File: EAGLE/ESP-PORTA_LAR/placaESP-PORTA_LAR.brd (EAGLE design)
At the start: 53.3 x 42.9 mm, 21 parts

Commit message: Correções na placa da porta
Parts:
- R1, R2, R3, R4, R5, R6, R7, R8: device resistor:0204/7 -> resistor:0207/10
- moved R7 13.9 mm to (44.2, 9.14)
- moved RESET 4.87 mm to (41.3, 20.1)
- moved FTDI 4.55 mm to (42.5, 38.7)
- moved FLASH 4.51 mm to (41.1, 28.6)
- moved MRFC522 2.57 mm to (49.1, 22.9)
- moved R8 2.43 mm to (32.0, 15.4)
- moved R4 1.73 mm to (6.86, 34.7)
- moved R2 1.65 mm to (3.81, 34.7)
- moved R5 1.05 mm to (32.0, 9.14)
- moved R3 0.74 mm to (31.1, 23.7)
- moved R6 0.57 mm to (32.0, 12.2)
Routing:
- net LED3: track 13.8 -> 36.3 mm
- net VCC: track 120.2 -> 104.1 mm
- net MISO: track 56.4 -> 40.7 mm, vias 1 -> 2
- net MOSI: track 37.4 -> 25.3 mm, vias 0 -> 1
- net CTS: track 65.5 -> 76.7 mm
- net RST: track 25.3 -> 35.7 mm, vias 0 -> 1
- net LED1: track 35.4 -> 43.4 mm
- net N$7: track 14.8 -> 7.53 mm
- net N$8: track 23.6 -> 16.4 mm
- net SDA: track 73.6 -> 80.5 mm, vias 1 -> 2
- net SCK: track 62.1 -> 67.2 mm
- net RXI: track 22.1 -> 25.8 mm
- net N$3: track 10.6 -> 13.0 mm
- net LED4: track 12.2 -> 10.6 mm
- net N$5: track 6.84 -> 8.39 mm
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
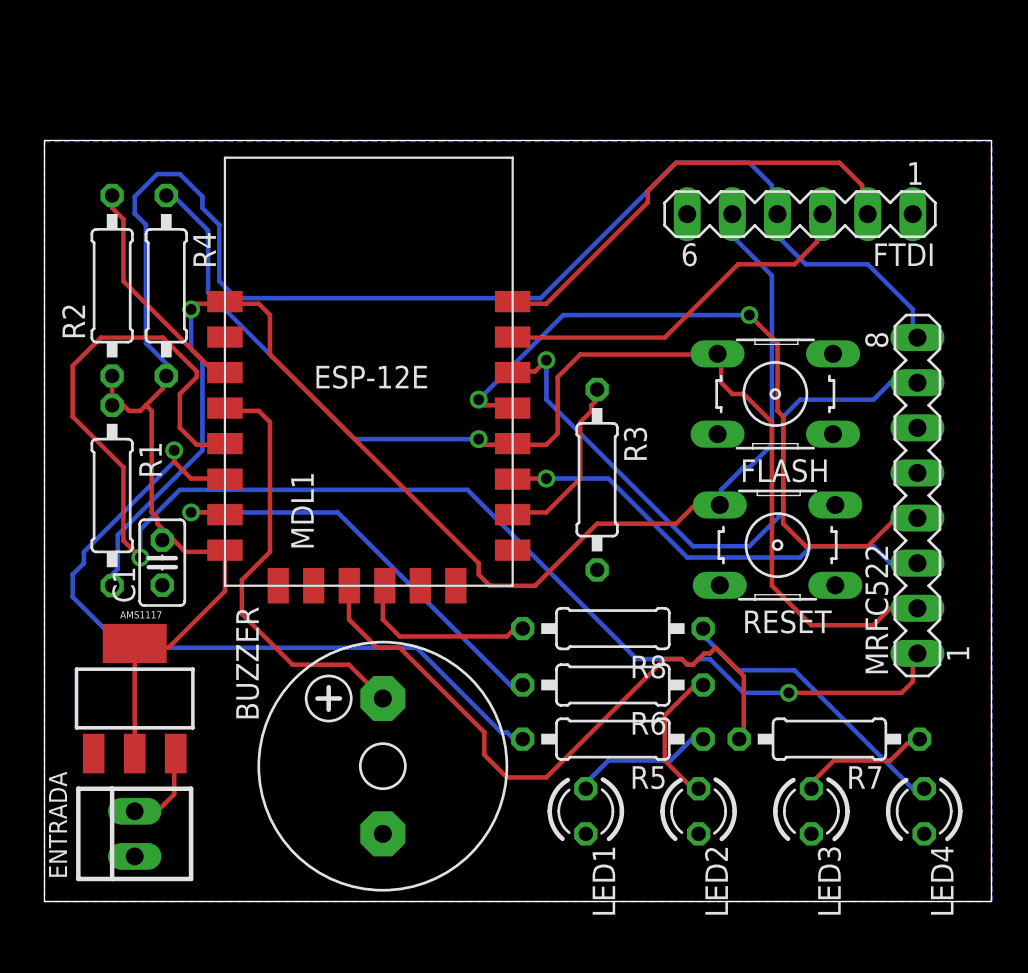
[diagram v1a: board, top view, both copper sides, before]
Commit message: Mudanças na placa
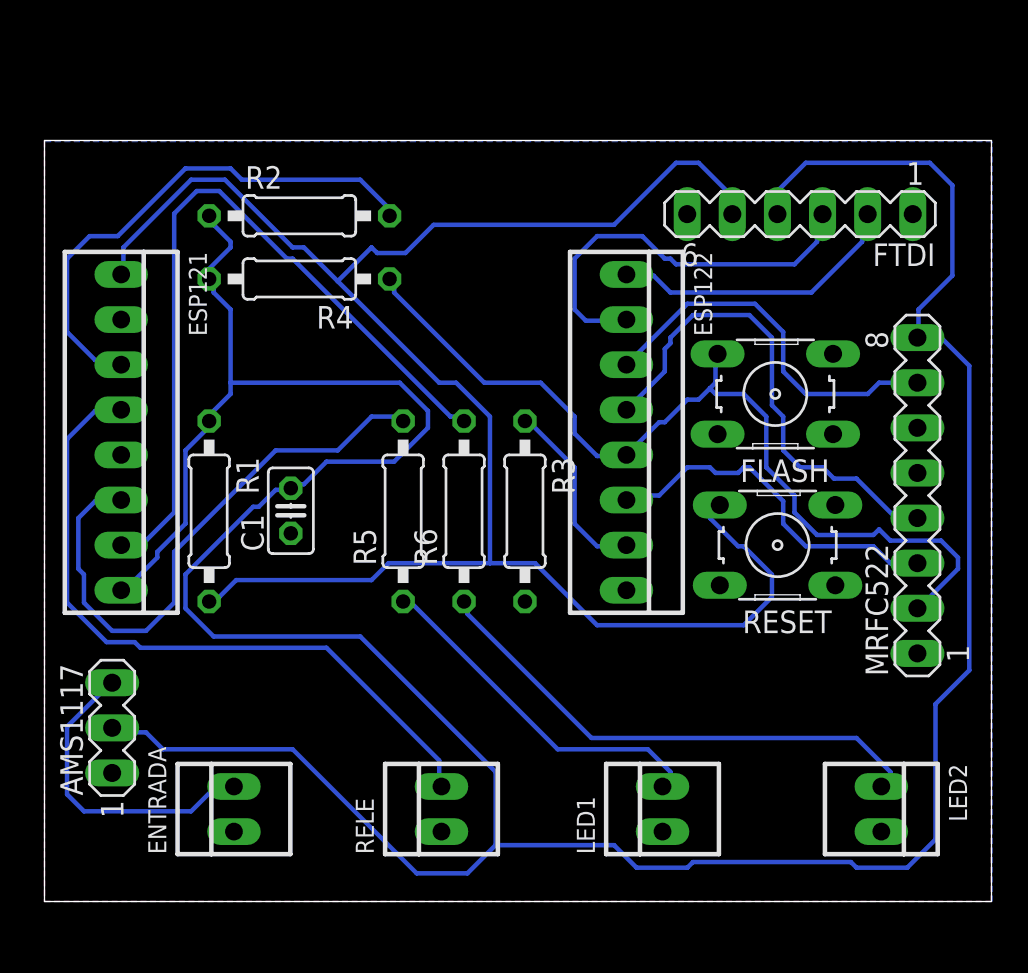
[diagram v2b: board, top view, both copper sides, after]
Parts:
- removed BUZZER: F/CM12P, buzzer:F/CM12P
- removed LED3, LED4: (no value), led:LED3MM
- removed MDL1: (no value), ESP8266-ESP12E:ESP8266-ESP12E
- removed R7, R8: 220R, resistor:0207/10
- added ESP121: Dir, con-molex:22-23-2081
- added ESP122: Esq, con-molex:22-23-2081
- added RELE: 2, con-molex:22-23-2021
- AMS1117: device kaibader:AMS1117 -> con-lstb:MA03-1
- ENTRADA: value 22-23-2021 -> 1
- LED1: value (none) -> 3; device led:LED3MM -> con-molex:22-23-2021
- LED2: value (none) -> 4; device led:LED3MM -> con-molex:22-23-2021
- moved R5 17.4 mm to (20.2, 22.0), turned to 90 degrees
- moved R6 12.9 mm to (23.6, 22.0), turned to 90 degrees
- moved R2 11.3 mm to (14.4, 38.6), turned to 0 degrees
- moved LED2 10.3 mm to (47.1, 5.21)
- moved C1 7.81 mm to (13.9, 22.0)
- moved R4 7.50 mm to (14.4, 35.1), turned to 180 degrees
- moved ENTRADA 5.76 mm to (10.7, 5.21)
- moved R1 5.53 mm to (9.27, 22.0)
- moved R3 4.44 mm to (27.1, 22.0)
- moved LED1 4.32 mm to (34.8, 5.21), turned to 90 degrees
- moved AMS1117 2.08 mm to (3.81, 9.78), turned to 90 degrees
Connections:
- removed net BUZZ: BUZZER.+, MDL1.4
- removed net LED3: MDL1.19, R7.2
- removed net LED4: MDL1.20, R8.2
- removed net N$7: LED3.A, R7.1
- removed net N$8: LED4.A, R8.1
- new net RELE: ESP121.4, RELE.2
- net CTS: now also ESP121.1; no longer MDL1.1
- net GND: now also AMS1117.1, ESP122.8, LED1.1, LED2.2, RELE.1; no longer AMS1117.GND, BUZZER.-, LED1.K, LED2.K, LED3.K, LED4.K, MDL1.9
- net IN+: now also AMS1117.3; no longer AMS1117.VIN
- net LED1: now also ESP121.6; no longer MDL1.6
- net LED2: now also ESP121.7; no longer MDL1.7
- net MISO: now also ESP122.4; no longer MDL1.13
- net MOSI: now also ESP122.6; no longer MDL1.11
- net N$1: now also ESP122.7; no longer MDL1.10
- net N$3: now also ESP121.3; no longer MDL1.3
- net N$5: now also LED1.2; no longer LED1.A
- net N$6: now also LED2.1; no longer LED2.A
- net RST: now also ESP122.3; no longer MDL1.14
- net RXI: now also ESP122.1; no longer MDL1.16
- net SCK: now also ESP122.5; no longer MDL1.12
- net SDA: now also ESP121.5; no longer MDL1.5
- net TXO: now also ESP122.2; no longer MDL1.15
- net VCC: now also AMS1117.2, ESP121.8; no longer AMS1117.HEATSINK, AMS1117.VOUT, MDL1.8
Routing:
- net VCC: track 104.1 -> 187.6 mm
- net SDA: track 80.5 -> 0.00 mm, vias 2 -> 0
- net RELE: track 0.00 -> 39.1 mm
- net LED3: track 36.3 -> 0.00 mm
- net CTS: track 76.7 -> 106.5 mm, vias 1 -> 0
- net BUZZ: track 24.3 -> 0.00 mm
- net N$6: track 8.11 -> 29.4 mm
- net LED2: track 25.2 -> 42.9 mm, vias 1 -> 0
- net N$3: track 13.0 -> 29.5 mm
- net N$8: track 16.4 -> 0.00 mm
- net SCK: track 67.2 -> 51.1 mm, vias 1 -> 0
- net RST: track 35.7 -> 21.5 mm, vias 1 -> 0
- net MISO: track 40.7 -> 27.6 mm, vias 2 -> 0
- net IN+: track 4.96 -> 17.8 mm
- net N$5: track 8.39 -> 20.0 mm
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
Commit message: Mais mod. na placa da porta
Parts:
- moved RESET 3.06 mm to (41.0, 17.0), turned to 270 degrees
- turned FLASH to 270 degrees
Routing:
- net CTS: track 106.5 -> 168.0 mm
- net SDA: track 0.00 -> 60.7 mm
- net LED2: track 42.9 -> 31.1 mm
- net LED1: track 33.1 -> 22.1 mm
- net N$3: track 29.5 -> 19.1 mm
- net TXO: track 23.1 -> 29.7 mm
- net MISO: track 27.6 -> 21.1 mm
- net VCC: track 187.6 -> 191.6 mm
- net RST: track 21.5 -> 18.1 mm
- net SCK: track 51.1 -> 48.3 mm
- net IN+: track 17.8 -> 20.0 mm
- net N$6: track 29.4 -> 27.8 mm
- net RELE: track 39.1 -> 37.6 mm
- net N$5: track 20.0 -> 18.9 mm
- net MOSI: track 20.4 -> 20.9 mm

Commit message: Nova Placa
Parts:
- ENTRADA: value 1 -> (none); device con-molex:22-23-2021 -> con-jack:SPC4077
- moved AMS1117 44.6 mm to (48.3, 13.7), turned to 270 degrees
- moved LED2 40.5 mm to (6.60, 4.32), turned to 90 degrees
- moved FTDI 39.9 mm to (3.97, 28.3), turned to 270 degrees
- moved ENTRADA 31.5 mm to (42.2, 5.08), turned to 180 degrees
- moved R6 22.4 mm to (2.92, 13.5)
- moved ESP121 20.3 mm to (20.1, 13.6), turned to 0 degrees
- moved ESP122 19.9 mm to (20.1, 41.8), turned to 0 degrees
- moved R2 18.5 mm to (15.7, 20.2), turned to 180 degrees
- moved LED1 15.9 mm to (18.9, 4.32)
- moved R5 15.8 mm to (6.86, 13.5)
- moved R1 15.1 mm to (24.3, 23.6), turned to 180 degrees
- moved R3 12.9 mm to (23.6, 34.4), turned to 0 degrees
- moved MRFC522 12.2 mm to (48.3, 35.1)
- moved C1 11.4 mm to (22.5, 29.6), turned to 270 degrees
- moved RELE 9.06 mm to (31.4, 4.32)
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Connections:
- removed net N$6: LED2.1, R6.1
- new net N$2: LED2.2, R6.1
- net GND: now also ENTRADA.2, LED2.1; no longer LED2.2
- net IN+: now also ENTRADA.3; no longer ENTRADA.2
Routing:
- net CTS: track 168.0 -> 57.1 mm
- net VCC: track 191.6 -> 154.7 mm
- net GND: track 0.00 -> 30.2 mm, vias 0 -> 10
- net N$6: track 27.8 -> 0.00 mm
- net SDA: track 60.7 -> 33.9 mm
- net LED2: track 31.1 -> 56.9 mm
- net RELE: track 37.6 -> 59.6 mm
- net RST: track 18.1 -> 37.1 mm
- net MISO: track 21.1 -> 38.0 mm
- net TXO: track 29.7 -> 17.1 mm
- net MOSI: track 20.9 -> 33.0 mm
- net N$3: track 19.1 -> 8.92 mm
- net SCK: track 48.3 -> 57.5 mm
- net N$5: track 18.9 -> 13.2 mm
- net N$2: track 0.00 -> 4.84 mm
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- removed copper zone on layer 1, net GND
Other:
- board size 53.3 x 42.9 mm -> 52.8 x 47.8 mm

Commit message: Últimas modificações
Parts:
- moved R2 1.73 mm to (17.1, 19.2)
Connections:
- net GND: no longer FLASH.2
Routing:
- net RELE: track 59.6 -> 19.1 mm
- net SDA: track 33.9 -> 65.0 mm
- net LED2: track 56.9 -> 28.7 mm
- net GND: track 30.2 -> 55.7 mm
- net MOSI: track 33.0 -> 53.5 mm
- net VCC: track 154.7 -> 150.0 mm
- net LED1: track 25.8 -> 21.2 mm
- net IN+: track 16.0 -> 11.7 mm
- net CTS: track 57.1 -> 59.8 mm
- net TXO: track 17.1 -> 19.1 mm
- net N$3: track 8.92 -> 7.41 mm
- net SCK: track 57.5 -> 58.8 mm
- net RST: track 37.1 -> 36.0 mm
- net RXI: track 13.6 -> 14.4 mm
